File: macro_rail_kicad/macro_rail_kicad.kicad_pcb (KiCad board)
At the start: 2 copper layers, 18 parts, among them J1 Battery, J2 Motor, J3 128x128 OLED, J4 GIMBAL, J5 2.5mm Plug, SW1 POWER, SW2 SHUTTER, SW3 PREVIOUS, SW4 NEXT, SW5 RESET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

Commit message: Finished draft of PCB
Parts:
- J4: footprint Connector_PinHeader_2.54mm:PinHeader_1x04_P2.54mm_Horizontal -> Connector_PinHeader_2.54mm:PinHeader_1x04_P2.54mm_Vertical
- J5: footprint Connector_PinHeader_2.54mm:PinHeader_1x02_P2.54mm_Horizontal -> Connector_PinHeader_2.54mm:PinHeader_1x02_P2.54mm_Vertical
- moved SW3 94.6 mm to (96.5, 114.3)
- moved SW2 92.5 mm to (96.5, 101.6)
- moved SW5 80.6 mm to (96.5, 88.9)
- moved J1 79.3 mm to (203.3, 74.9), turned to 90 degrees
- moved C1 66.7 mm to (182.9, 80.0), turned to 90 degrees
- moved U1 60.9 mm to (181.6, 108.0), turned to -90 degrees
- moved C2 56.1 mm to (177.8, 83.9), turned to -90 degrees
- moved C3 54.6 mm to (177.8, 91.4), turned to 90 degrees
- moved SW1 53.8 mm to (200.7, 80.4)
- moved SW4 52.4 mm to (144.8, 114.3)
- moved A1 39.0 mm to (172.7, 78.7), turned to -90 degrees
- moved J3 38.6 mm to (116.5, 76.2)
- moved U2 36.5 mm to (182.9, 86.4), turned to -90 degrees
- moved U3 30.6 mm to (143.5, 94.0), turned to 90 degrees
- moved J5 27.0 mm to (148.6, 82.5), turned to -90 degrees
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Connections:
- J5 pad 1: (no net) -> Net-(J5-Pad1)
- J5 pad 2: (no net) -> Net-(J5-Pad2)
- SW1 pad 1: Net-(J1-Pin_2) -> VBAT
- SW1 pad 2: VBAT -> Net-(J1-Pin_2)
- SW1 pad 3: (no net) -> unconnected-(SW1-C-Pad3)
- SW1 pad 4: (no net) -> VBAT
- SW1 pad 5: (no net) -> Net-(J1-Pin_2)
- SW1 pad 6: (no net) -> unconnected-(SW1-C-Pad6)
- U1 pad 10: B_SHUT -> B_NEXT
- U1 pad 12: B_NEXT -> B_SHUT
- U1 pad 14: M_RST -> M_DIR
- U1 pad 15: M_SLP -> M_STEP
- U1 pad 16: M_STEP -> M_SLP
- U1 pad 17: M_DIR -> M_RST
- U1 pad 31: GIMB_X -> GIMB_Y
- U1 pad 32: GIMB_Y -> GIMB_X
- U3 pad 4: Net-(J5-PadG) -> Net-(J5-Pad1)
- U3 pad 5: Net-(J5-PadT) -> Net-(J5-Pad2)
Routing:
- net GND: track 0.00 -> 358.5 mm
- net 5V: track 0.00 -> 133.2 mm
- net RESET: track 0.00 -> 126.9 mm
- net B_PREV: track 0.00 -> 90.7 mm, vias 0 -> 2
- net B_SHUT: track 0.00 -> 83.9 mm, vias 0 -> 2
- net OLED_RST: track 0.00 -> 83.1 mm, vias 0 -> 2
- net OLED_DC: track 0.00 -> 78.9 mm, vias 0 -> 2
- net OLED_CS: track 0.00 -> 78.2 mm
- net OLED_SDA: track 0.00 -> 74.6 mm, vias 0 -> 2
- net OLED_SCL: track 0.00 -> 70.3 mm
- net VBAT: track 0.00 -> 59.8 mm
- net B_NEXT: track 0.00 -> 45.1 mm, vias 0 -> 1
- net GIMB_VDD: track 0.00 -> 14.1 mm
- net Net-(J1-Pin_2): track 0.00 -> 12.5 mm
- net GIMB_GND: track 0.00 -> 8.67 mm
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- added copper zone on B.Cu, net GND
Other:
- board outline added: 119.4 x 57.2 mm

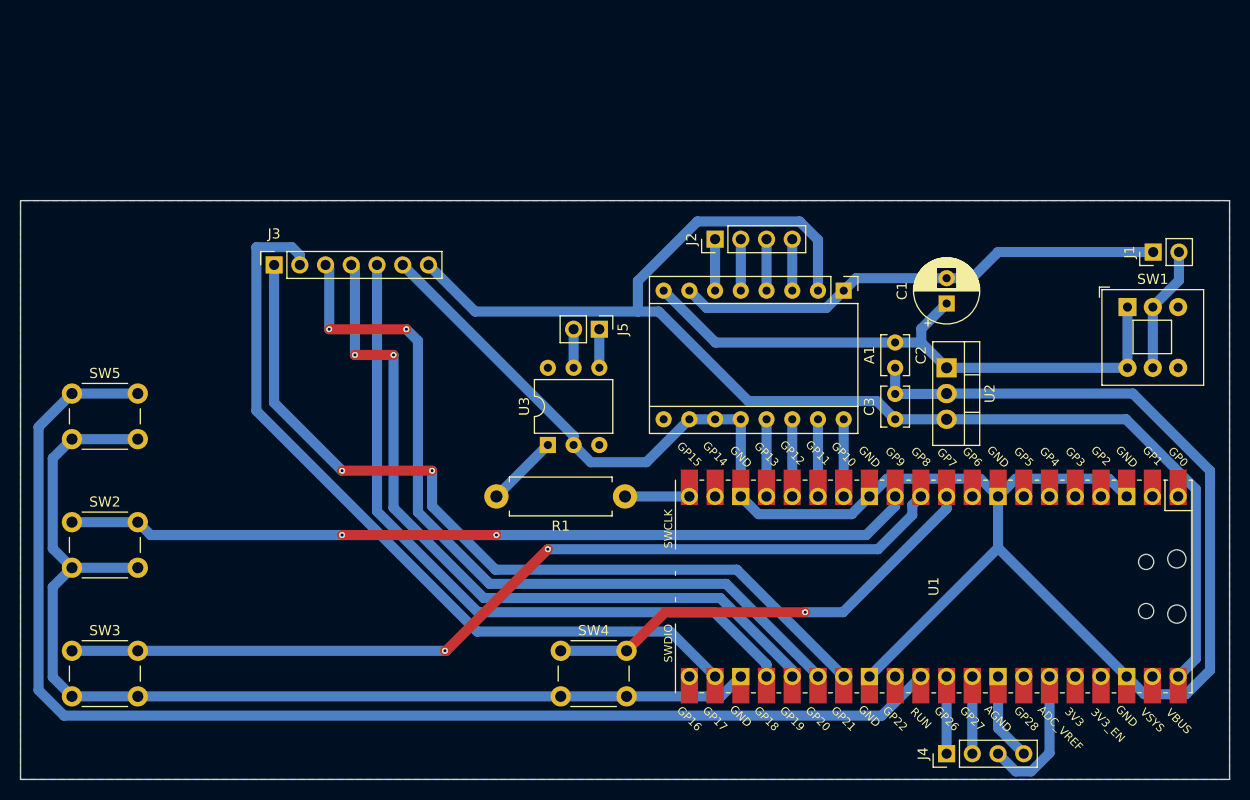
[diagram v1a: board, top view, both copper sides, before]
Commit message: Added mounting holes.  Fixed DRC violations.
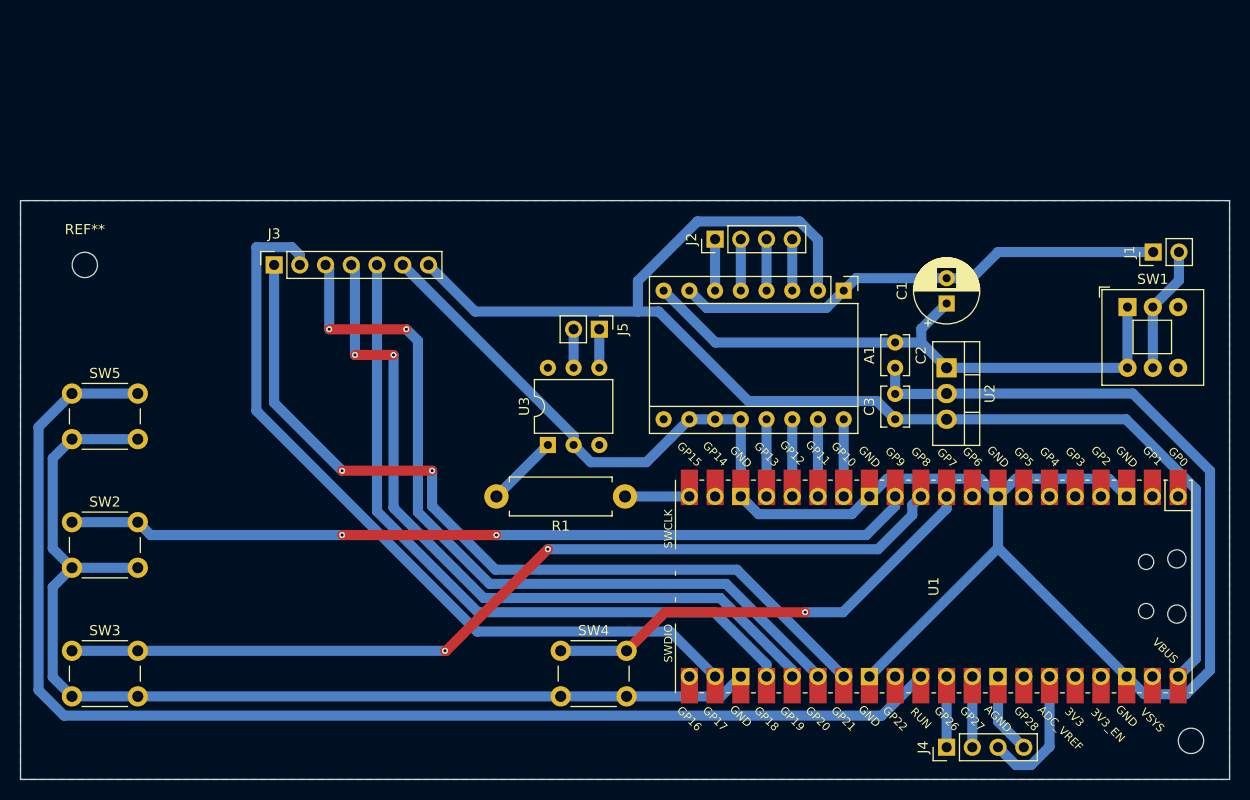
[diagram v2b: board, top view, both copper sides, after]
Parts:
- added REF**: MountingHole_2.5mm, MountingHole:MountingHole_2.5mm, F.Cu at (97.8, 76.2)
- added REF**: MountingHole_2.5mm, MountingHole:MountingHole_2.5mm, F.Cu at (207.0, 123.2)
- moved J4 0.63 mm to (182.9, 123.8)
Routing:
- net GIMB_VDD: track 14.1 -> 13.5 mm
- net GIMB_GND: track 8.67 -> 8.04 mm
- net GIMB_Y: track 7.62 -> 6.98 mm
- net GIMB_X: track 7.62 -> 6.98 mm

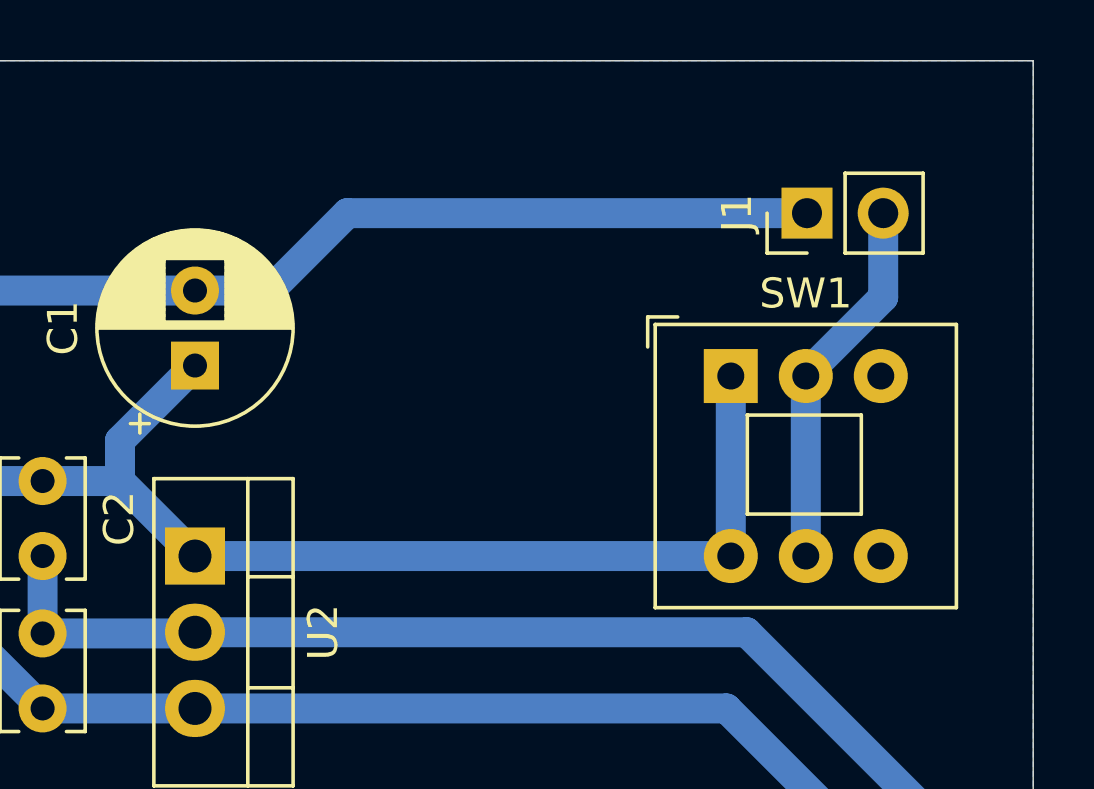
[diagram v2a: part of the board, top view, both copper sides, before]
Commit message: README links updates.  Removed power switch (amps too low)
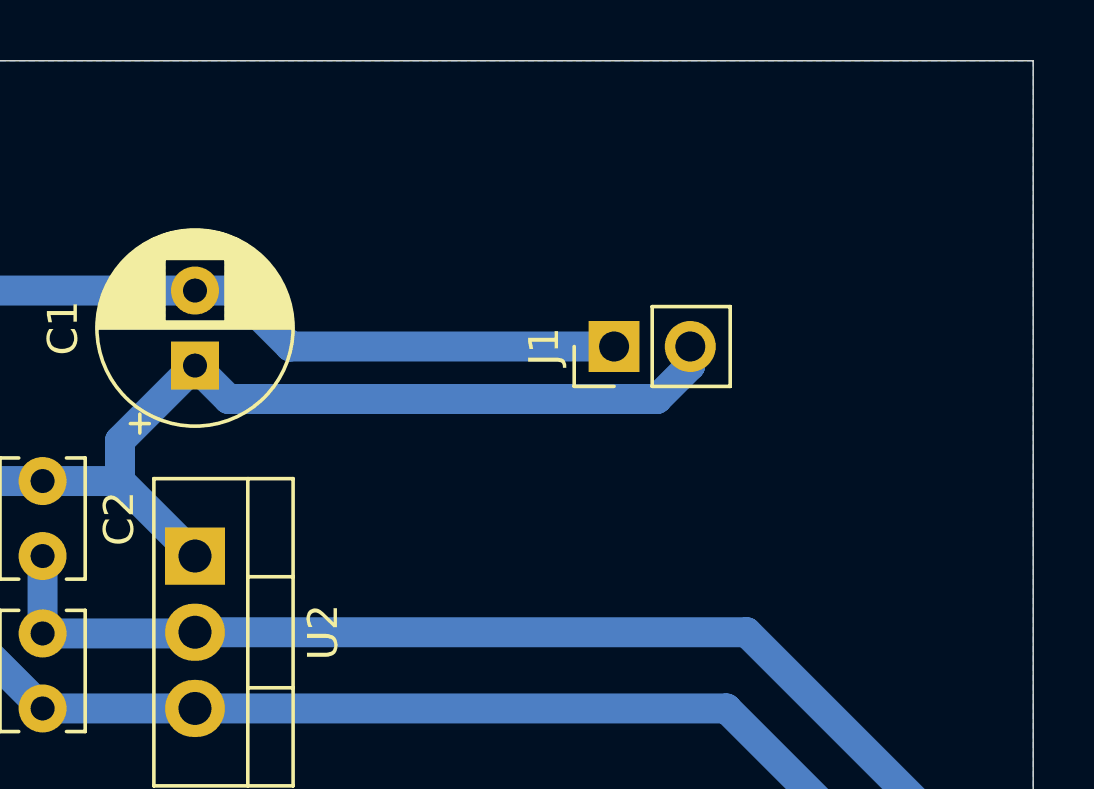
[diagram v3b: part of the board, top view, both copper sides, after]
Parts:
- removed SW1: POWER, Button_Switch_THT:SW_Push_2P2T_Toggle_CK_PVA2OAH5xxxxxxV2
- moved J1 7.82 mm to (196.8, 79.4)
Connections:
- J1 pad 2: Net-(J1-Pin_2) -> VBAT
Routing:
- net Net-(J1-Pin_2): track 12.5 -> 0.00 mm
- net GND: track 358.5 -> 351.8 mm
- net VBAT: track 59.8 -> 54.1 mm

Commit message: Added pcb exports.
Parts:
- added REF**: MountingHole_2.5mm, MountingHole:MountingHole_2.5mm, F.Cu at (207.0, 76.2)
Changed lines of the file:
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@@
 		(pad_to_mask_clearance 0)
 		(allow_soldermask_bridges_in_footprints no)
+		(grid_origin 91.44 69.85)
 		(pcbplotparams
-			(layerselection 0x00010fc_ffffffff)
+			(layerselection 0x0001000_fffffffe)
 			(plot_on_all_layers_selection 0x0000000_00000000)
 			(disableapertmacros no)
@@
 			(viasonmask no)
 			(mode 1)
-			(useauxorigin no)
+			(useauxorigin yes)
 			(hpglpennumber 1)
 			(hpglpenspeed 20)
@@
 			(outputformat 1)
 			(mirror no)
-			(drillshape 1)
+			(drillshape 0)
 			(scaleselection 1)
-			(outputdirectory "")
+			(outputdirectory "export/")
 		)
 	)
@@
 		)
 	)
+	(footprint "MountingHole:MountingHole_2.5mm"
+		(layer "F.Cu")
+		(at 207.01 76.2)
+		(descr "Mounting Hole 2.5mm, no annular")
+		(tags "mounting hole 2.5mm no annular")
+		(property "Reference" "REF**"
+			(at 0 -3.5 0)
+			(layer "F.SilkS")
+			(hide yes)
+			(effects
+				(font
+					(size 1 1)
+					(thickness 0.15)
+				)
+			)
+		)
+		(property "Value" "MountingHole_2.5mm"
+			(at 0 3.5 0)
+			(layer "F.Fab")
+			(hide yes)
+			(effects
+				(font
+					(size 1 1)
+					(thickness 0.15)
+				)
+			)
+		)
+		(property "Footprint" "MountingHole:MountingHole_2.5mm"
+			(at 0 0 0)
+			(unlocked yes)
+			(layer "F.Fab")
+			(hide yes)
+			(effects
+				(font
+					(size 1.27 1.27)
+					(thickness 0.15)
+				)
+			)
+		)
+		(property "Datasheet" ""
+			(at 0 0 0)
+			(unlocked yes)
+			(layer "F.Fab")
+			(hide yes)
+			(effects
+				(font
+					(size 1.27 1.27)
+					(thickness 0.15)
+				)
+			)
+		)
+		(property "Description" ""
+			(at 0 0 0)
+			(unlocked yes)
+			(layer "F.Fab")
+			(hide yes)
+			(effects
+				(font
+					(size 1.27 1.27)
+					(thickness 0.15)
+				)
+			)
+		)
+		(attr exclude_from_pos_files exclude_from_bom)
+		(fp_circle
+			(center 0 0)
+			(end 2.5 0)
+			(stroke
+				(width 0.15)
+				(type solid)
+			)
+			(fill none)
+			(layer "Cmts.User")
+		)
+		(fp_circle
+			(center 0 0)
+			(end 2.75 0)
+			(stroke
+				(width 0.05)
+				(type solid)
+			)
+			(fill none)
+			(layer "F.CrtYd")
+		)
+		(fp_text user "${REFERENCE}"
+			(at 0 0 0)
+			(layer "F.Fab")
+			(effects
+				(font
+					(size 1 1)
+					(thickness 0.15)
+				)
+			)
+		)
+		(pad "" np_thru_hole circle
+			(at 0 0)
+			(size 2.5 2.5)
+			(drill 2.5)
+			(layers "*.Cu" "*.Mask")
+		)
+	)
 	(footprint "Connector_PinHeader_2.54mm:PinHeader_1x04_P2.54mm_Vertical"
 		(layer "F.Cu")
@@
 			(at 0 -3.5 0)
 			(layer "F.SilkS")
+			(hide yes)
 			(effects
 				(font
@@
 			(layer "F.CrtYd")
 		)
-		(fp_text user "${REFERENCE}"
-			(at 0 0 0)
-			(layer "F.Fab")
-			(effects
-				(font
-					(size 1 1)
-					(thickness 0.15)
-				)
-			)
-		)
 		(pad "" np_thru_hole circle

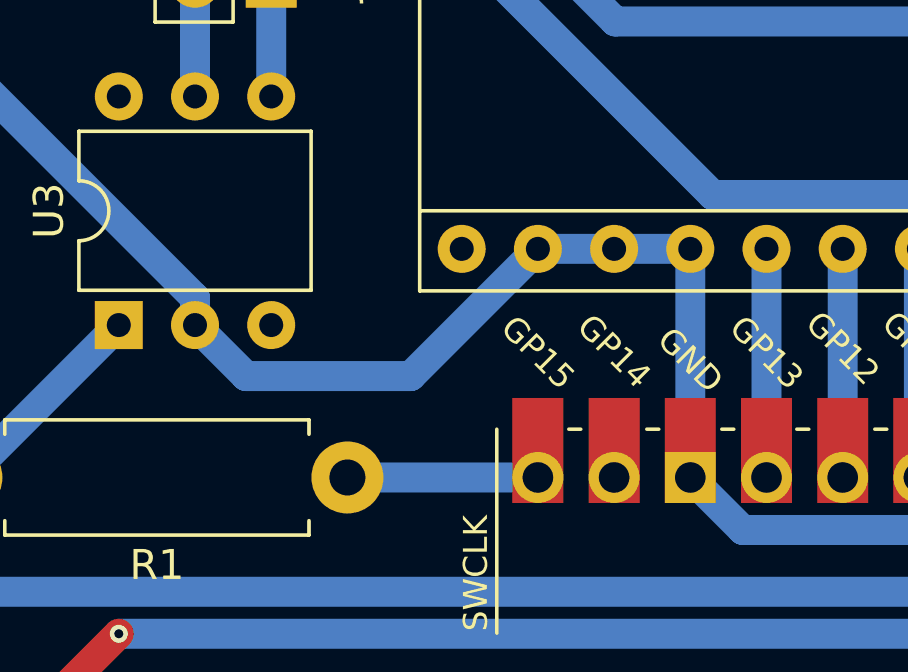
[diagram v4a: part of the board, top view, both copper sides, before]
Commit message: Updated schmatic and pcb for microstepping
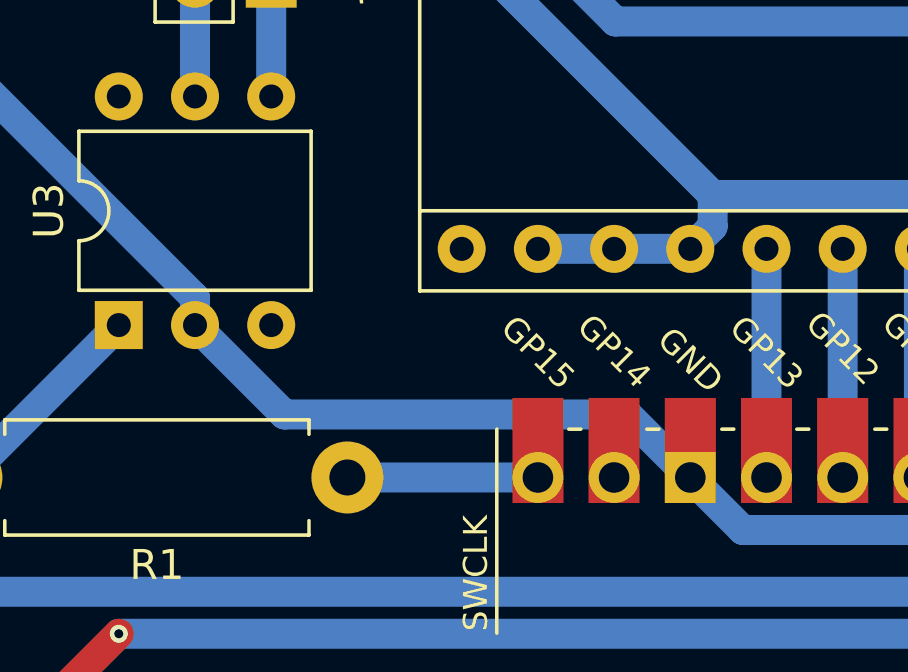
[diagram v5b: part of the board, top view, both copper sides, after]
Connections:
- A1 pad 10: GND -> 5V
- A1 pad 11: GND -> 5V
- A1 pad 12: GND -> 5V
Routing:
- net GND: track 351.8 -> 343.8 mm
- net 5V: track 133.2 -> 140.4 mm
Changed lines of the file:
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@@
 			(layers "*.Cu" "*.Mask")
 			(remove_unused_layers no)
-			(net 3 "GND")
+			(net 32 "5V")
 			(pinfunction "MS1")
 			(pintype "input")
@@
 			(layers "*.Cu" "*.Mask")
 			(remove_unused_layers no)
-			(net 3 "GND")
+			(net 32 "5V")
 			(pinfunction "MS2")
 			(pintype "input")
@@
 			(layers "*.Cu" "*.Mask")
 			(remove_unused_layers no)
-			(net 3 "GND")
+			(net 32 "5V")
 			(pinfunction "MS3")
 			(pintype "input")
@@
 	)
 	(segment
+		(start 160.46 96.96)
+		(end 162.56 99.06)
+		(width 1)
+		(layer "B.Cu")
+		(net 3)
+	)
+	(segment
 		(start 94.62 116.9)
 		(end 94.62 108)
@@
 	)
 	(segment
+		(start 146.05 93.98)
+		(end 149.03 96.96)
+		(width 1)
+		(layer "B.Cu")
+		(net 3)
+	)
+	(segment
 		(start 162.56 116.84)
 		(end 160.6 118.8)
@@
 	)
 	(segment
-		(start 157.48 91.44)
-		(end 153.24 95.68)
-		(width 1)
-		(layer "B.Cu")
-		(net 3)
-	)
-	(segment
 		(start 187.96 99.06)
 		(end 189.71 97.31)
@@
 	)
 	(segment
+		(start 149.03 96.96)
+		(end 160.46 96.96)
+		(width 1)
+		(layer "B.Cu")
+		(net 3)
+	)
+	(segment
 		(start 201.27 88.9)
 		(end 208.89 96.52)
@@
 	)
 	(segment
-		(start 162.56 99.06)
-		(end 162.56 91.44)
-		(width 1)
-		(layer "B.Cu")
-		(net 3)
-	)
-	(segment
 		(start 157.48 78.74)
 		(end 159.18 80.44)
@@
 	)
 	(segment
-		(start 147.75 95.68)
-		(end 146.05 93.98)
-		(width 1)
-		(layer "B.Cu")
-		(net 3)
-	)
-	(segment
-		(start 157.48 91.44)
-		(end 162.56 91.44)
-		(width 1)
-		(layer "B.Cu")
-		(net 3)
-	)
-	(segment
 		(start 177.8 88.94)
 		(end 182.84 88.94)
@@
 		(start 175.26 99.06)
 		(end 177.01 97.31)
-		(width 1)
-		(layer "B.Cu")
-		(net 3)
-	)
-	(segment
-		(start 153.24 95.68)
-		(end 147.75 95.68)
 		(width 1)
 		(layer "B.Cu")
@@
 	)
 	(segment
+		(start 163.304164 89.644164)
+		(end 163.304164 90.695836)
+		(width 1)
+		(layer "B.Cu")
+		(net 32)
+	)
+	(segment
 		(start 152.4 80.8)
 		(end 154.46 80.8)
@@
 		(width 1)
 		(layer "B.Cu")
+		(net 32)
+	)
+	(segment
+		(start 162.56 91.44)
+		(end 157.48 91.44)
+		(width 1)
+		(layer "B.Cu")
+		(net 32)
+	)
+	(segment
+		(start 163.304164 90.695836)
+		(end 162.56 91.44)
+		(width 1)
+		(layer "B.Cu")
